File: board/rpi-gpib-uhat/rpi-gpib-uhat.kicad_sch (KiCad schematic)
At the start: 39 parts, among them J1 RPI_GPIO, J2 GPIB, U1 SN75160BDW, U2 SN75162BDW, U3 LM317_SOT-223, U4 CAT24C32

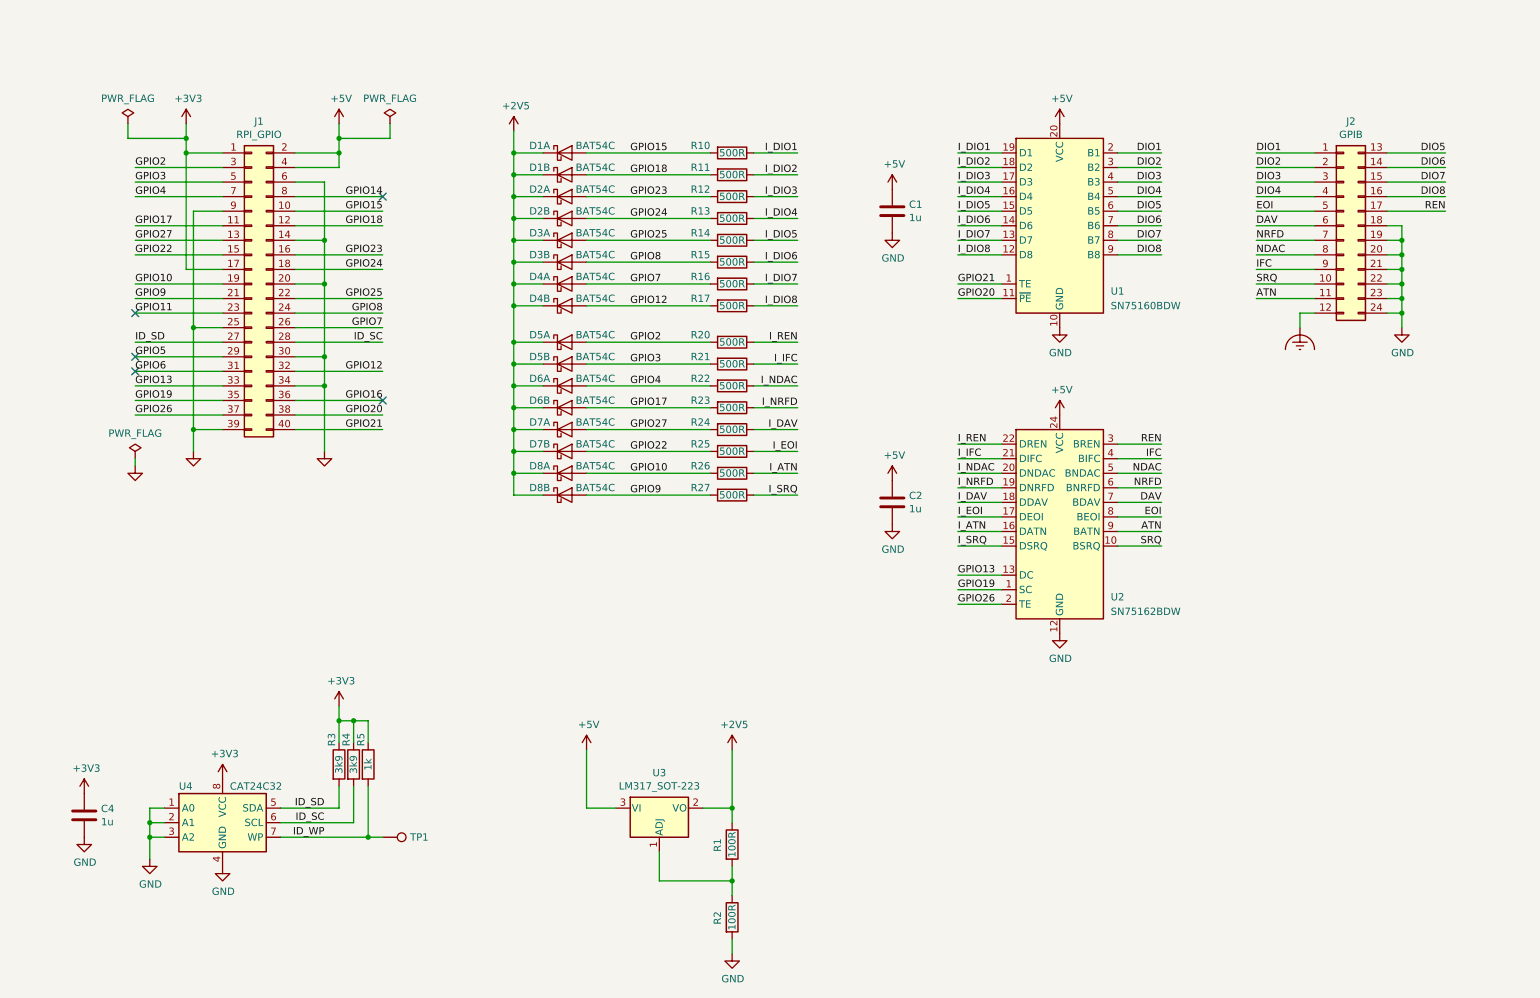
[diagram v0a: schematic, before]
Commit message: Change uHAT pinout and re-route.
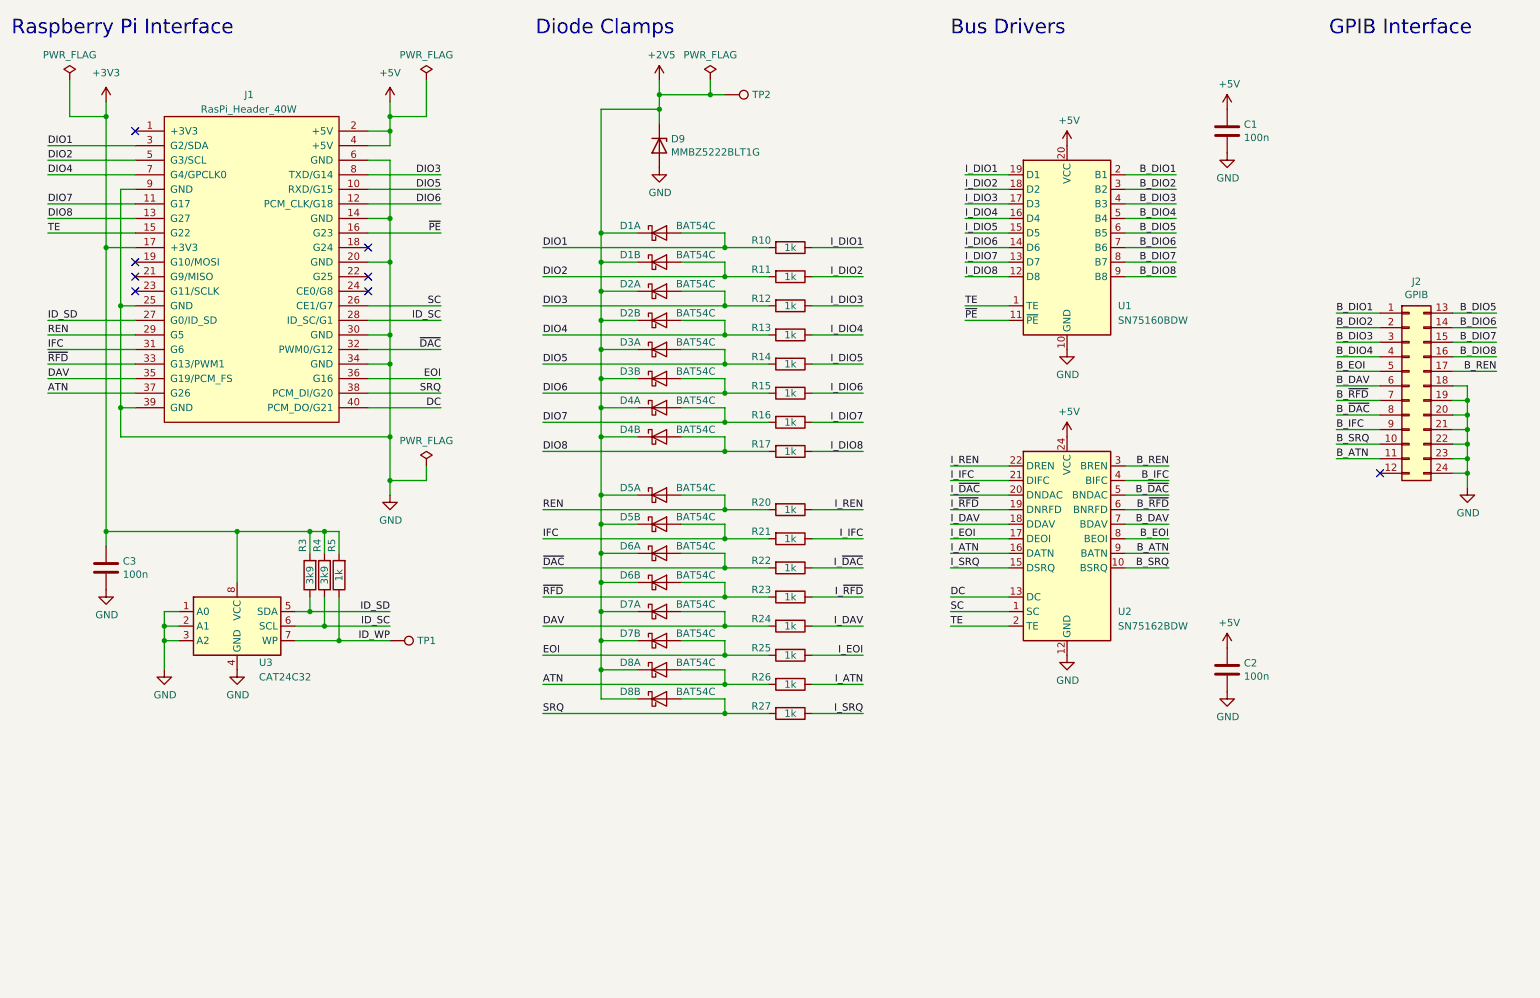
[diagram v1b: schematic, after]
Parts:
- removed C4: 1u, Capacitor_SMD:C_0805_2012Metric, symbol Device:C
- removed J1: RPI_GPIO, lib:PinSocket_2x20_P2.54mm_Vertical_Centered_Anchor, symbol Connector_Generic:Conn_02x20_Odd_Even
- removed R1, R2: 100R, Resistor_SMD:R_0402_1005Metric, symbol Device:R
- removed U3: LM317_SOT-223, Package_TO_SOT_SMD:SOT-223-3_TabPin2, symbol Regulator_Linear:LM317_SOT-223
- removed U4: CAT24C32, Package_SO:SOIC-8_3.9x4.9mm_P1.27mm, symbol Memory_EEPROM:CAT24C128
- added C3: 100n, Capacitor_SMD:C_0402_1005Metric, symbol Device:C
- added D9: MMBZ5222BLT1G, Package_TO_SOT_SMD:SC-59, symbol Device:D_Zener
- added J1: RasPi_Header_40W, local:PinSocket_2x20_P2.54mm_Vertical_Centered_Anchor, symbol local:RasPi_Header_40W
- added TP2: TestPoint, TestPoint:TestPoint_Pad_D1.0mm, symbol Connector:TestPoint
- added U3: CAT24C32, Package_SO:SOIC-8_3.9x4.9mm_P1.27mm, symbol Memory_EEPROM:CAT24C128
- C1, C2: value 1u -> 100n; footprint Capacitor_SMD:C_0805_2012Metric -> Capacitor_SMD:C_0402_1005Metric
- J2: footprint local:NorComp_111-024-113L001 -> local:NorComp_111-024-113L001_NoScrews
- R10, R11, R12, R13, R14, R15, R16, R17, R20, R21, R22, R23, R24, R25, R26, R27: value 500R -> 1k
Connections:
- net GPIO10 is gone; now on net ATN: D8.1 (A), R26.2
- net GPIO12 is gone; now on net DIO8: D4.2 (A), R17.2
- net GPIO15 is gone; now on net DIO1: D1.1 (A), R10.2
- net GPIO18 is gone; now on net DIO2: D1.2 (A), R11.2
- net GPIO2 is gone; now on net REN: D5.1 (A), R20.2
- net GPIO22 is gone; now on net EOI: D7.2 (A), R25.2
- net GPIO23 is gone; now on net DIO3: D2.1 (A), R12.2
- net GPIO24 is gone; now on net DIO4: D2.2 (A), R13.2
- net GPIO25 is gone; now on net DIO5: D3.1 (A), R14.2
- net GPIO26 is gone; now on net TE: U2.2 (TE)
- net GPIO27 is gone; now on net DAV: D7.1 (A), R24.2
- net GPIO3 is gone; now on net IFC: D5.2 (A), R21.2
- net GPIO7 is gone; now on net DIO7: D4.1 (A), R16.2
- net GPIO8 is gone; now on net DIO6: D3.2 (A), R15.2
- net GPIO9 is gone; now on net SRQ: D8.2 (A), R27.2
- net +2V5: now also D9.1 (K), TP2.1
- net +3V3: now also R3.2, R4.2, R5.2, C3.1, J1.17 (+3V3), U3.8 (VCC); no longer R3.1, R4.1, R5.1
- net +5V: now also J1.2 (+5V), J1.4 (+5V)
- net ATN: now also J1.37 (G26); no longer J2.11 (Pin_11), U2.9 (BATN)
- net DAV: now also J1.35 (G19/PCM_FS); no longer J2.6 (Pin_6), U2.7 (BDAV)
- net DIO1: now also J1.3 (G2/SDA); no longer J2.1 (Pin_1), U1.2 (B1)
- net DIO2: now also J1.5 (G3/SCL); no longer J2.2 (Pin_2), U1.3 (B2)
- net DIO3: now also J1.8 (TXD/G14); no longer J2.3 (Pin_3), U1.4 (B3)
- net DIO4: now also J1.7 (G4/GPCLK0); no longer J2.4 (Pin_4), U1.5 (B4)
- net DIO5: now also J1.10 (RXD/G15); no longer J2.13 (Pin_13), U1.6 (B5)
- net DIO6: now also J1.12 (PCM_CLK/G18); no longer J2.14 (Pin_14), U1.7 (B6)
- net DIO7: now also J1.11 (G17); no longer J2.15 (Pin_15), U1.8 (B7)
- net DIO8: now also J1.13 (G27); no longer J2.16 (Pin_16), U1.9 (B8)
- net EOI: now also J1.36 (G16); no longer J2.5 (Pin_5), U2.8 (BEOI)
- net GND: now also C3.2, D9.2 (A), J1.14 (GND), J1.20 (GND), J1.25 (GND), J1.30 (GND), J1.34 (GND), J1.39 (GND), J1.6 (GND), J1.9 (GND), U3.1 (A0), U3.2 (A1), U3.3 (A2), U3.4 (GND)
- net ID_SC: now also R4.1, J1.28 (ID_SC/G1), U3.6 (SCL); no longer R4.2
- net ID_SD: now also R3.1, J1.27 (G0/ID_SD), U3.5 (SDA); no longer R3.2
- net ID_WP: now also R5.1, U3.7 (WP); no longer R5.2
- net IFC: now also J1.31 (G6); no longer J2.9 (Pin_9), U2.4 (BIFC)
- net REN: now also J1.29 (G5); no longer J2.17 (Pin_17), U2.3 (BREN)
- net SRQ: now also J1.38 (PCM_DI/G20); no longer J2.10 (Pin_10), U2.10 (BSRQ)
- net Earth_Clean: no longer names the net of J2.12 (Pin_12)
- net GPIO13 renamed DC
- net DC: now also J1.40 (PCM_DO/G21)
- net GPIO17 renamed ~{RFD}
- net ~{RFD}: now also J1.33 (G13/PWM1)
- net GPIO19 renamed SC
- net SC: now also J1.26 (CE1/G7)
- net GPIO20 renamed ~{PE}
- net ~{PE}: now also J1.16 (G23)
- net GPIO21 renamed TE
- net TE: now also J1.15 (G22)
- net GPIO4 renamed ~{DAC}
- net ~{DAC}: now also J1.32 (PWM0/G12)
- net I_NDAC renamed I_~{DAC}
- net I_NRFD renamed I_~{RFD}
- net NDAC renamed B_~{DAC}
- net NRFD renamed B_~{RFD}
- new net B_ATN: J2.11 (Pin_11), U2.9 (BATN)
- new net B_DAV: J2.6 (Pin_6), U2.7 (BDAV)
- new net B_DIO1: J2.1 (Pin_1), U1.2 (B1)
- new net B_DIO2: J2.2 (Pin_2), U1.3 (B2)
- new net B_DIO3: J2.3 (Pin_3), U1.4 (B3)
- new net B_DIO4: J2.4 (Pin_4), U1.5 (B4)
- new net B_DIO5: J2.13 (Pin_13), U1.6 (B5)
- new net B_DIO6: J2.14 (Pin_14), U1.7 (B6)
- new net B_DIO7: J2.15 (Pin_15), U1.8 (B7)
- new net B_DIO8: J2.16 (Pin_16), U1.9 (B8)
- new net B_EOI: J2.5 (Pin_5), U2.8 (BEOI)
- new net B_IFC: J2.9 (Pin_9), U2.4 (BIFC)
- new net B_REN: J2.17 (Pin_17), U2.3 (BREN)
- new net B_SRQ: J2.10 (Pin_10), U2.10 (BSRQ)
- no-connect marks 5 -> 8
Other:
- note added: "Bus Drivers"
- note added: "Diode Clamps"
- note added: "GPIB Interface"
- note added: "Raspberry Pi Interface"

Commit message: Add FET switch for bus drivers.
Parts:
- added D9: BAT54C, Package_TO_SOT_SMD:SOT-23, symbol local:D_Schottky_x2_KCom_AAK_Split
- added Q1: BSH105, Package_TO_SOT_SMD:SOT-23, symbol Transistor_FET:BSS138
- added R28: 1k, Resistor_SMD:R_0402_1005Metric, symbol Device:R
- renumbered D9 to D10
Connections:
- net +2V5: now also D9.3 (K)
- net +5V: now also Q1.3 (D); no longer C1.1, C2.1, U1.20 (VCC), U2.24 (VCC)
- net B_IFC: now also R28.1
- net SC: now also J1.24 (CE0/G8); no longer J1.26 (CE1/G7)
- net TE: now also J1.23 (G11/SCLK); no longer J1.15 (G22)
- new net: C1.1, C2.1, Q1.2 (S), U1.20 (VCC), U2.24 (VCC)
- new net IFC_DET: D9.1 (A), J1.26 (CE1/G7), R28.2
- new net ON_BUS: J1.15 (G22), Q1.1 (G)
- no-connect marks 8 -> 5
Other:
- moved on the sheet: C1, C2, D10, D1A, D1B, D2A, D2B, D3A, D3B, D4A, D4B, D5A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
